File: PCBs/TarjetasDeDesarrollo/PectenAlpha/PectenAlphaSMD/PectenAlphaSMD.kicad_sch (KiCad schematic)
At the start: 26 parts, among them J1 ICSP, J2 GPIO, Q1 PN2222A, SW1 SW_Push, SW2 SW_DIP_x04, U1 PIC_8-14-18-20, U2 D148K

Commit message: Se actualizó la biblioteca de la pecten Alpha pero se harán modificaciones para el CH340 usb a ttl
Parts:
- BZ1: footprint (none) -> Buzzer_Beeper:Buzzer_12x9.5RM7.6
- D1: footprint (none) -> LED_SMD:LED_1206_3216Metric
- D10: footprint (none) -> LED_SMD:LED_RGB_5050-6
- J1: footprint (none) -> Connector_PinHeader_2.54mm:PinHeader_1x06_P2.54mm_Horizontal
- J2: footprint (none) -> Connector_PinHeader_2.54mm:PinHeader_2x12_P2.54mm_Vertical
- JP1: footprint (none) -> Jumper:SolderJumper-3_P1.3mm_Open_RoundedPad1.0x1.5mm
- R1, R10, R11, R12, R13, R14, R2, R3, R4, R5, R6, R7, R8, R9: footprint (none) -> Resistor_SMD:R_0805_2012Metric_Pad1.20x1.40mm_HandSolder
- RV1: footprint (none) -> Potentiometer_THT:Potentiometer_Runtron_RM-065_Vertical
- SW1: footprint (none) -> Button_Switch_THT:SW_PUSH_6mm_H4.3mm
- SW2: footprint (none) -> Button_Switch_THT:SW_DIP_SPSTx04_Slide_6.7x11.72mm_W7.62mm_P2.54mm_LowProfile
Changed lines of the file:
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@@
 			)
 		)
-		(property "Footprint" ""
+		(property "Footprint" "Resistor_SMD:R_0805_2012Metric_Pad1.20x1.40mm_HandSolder"
 			(at 142.494 145.796 90)
 			(effects
@@
 			)
 		)
-		(property "Footprint" ""
+		(property "Footprint" "Button_Switch_THT:SW_DIP_SPSTx04_Slide_6.7x11.72mm_W7.62mm_P2.54mm_LowProfile"
 			(at 99.06 68.58 0)
 			(effects
@@
 			)
 		)
-		(property "Footprint" ""
+		(property "Footprint" "Resistor_SMD:R_0805_2012Metric_Pad1.20x1.40mm_HandSolder"
 			(at 171.196 86.614 90)
 			(effects
@@
 			)
 		)
-		(property "Footprint" ""
+		(property "Footprint" "LED_SMD:LED_1206_3216Metric"
 			(at 114.3 115.57 0)
 			(effects
@@
 			)
 		)
-		(property "Footprint" ""
+		(property "Footprint" "Connector_PinHeader_2.54mm:PinHeader_2x12_P2.54mm_Vertical"
 			(at 105.41 163.83 0)
 			(effects
@@
 			)
 		)
-		(property "Footprint" ""
+		(property "Footprint" "Buzzer_Beeper:Buzzer_12x9.5RM7.6"
 			(at 128.905 80.01 90)
 			(effects
@@
 		(dnp no)
 		(fields_autoplaced yes)
-		(property "Reference" "#PWR?"
+		(property "Reference" "#PWR0101"
 			(at 99.06 186.69 0)
 			(effects
@@
 			(project ""
 				(path "/6ae505d1-4155-497e-9091-07ebabfd0d72"
-					(reference "#PWR?")
+					(reference "#PWR0101")
 					(unit 1)
 				)
@@
 			)
 		)
-		(property "Footprint" ""
+		(property "Footprint" "Potentiometer_THT:Potentiometer_Runtron_RM-065_Vertical"
 			(at 82.55 93.98 0)
 			(effects
@@
 			)
 		)
-		(property "Footprint" ""
+		(property "Footprint" "Jumper:SolderJumper-3_P1.3mm_Open_RoundedPad1.0x1.5mm"
 			(at 123.19 55.88 0)
 			(effects
@@
 			)
 		)
-		(property "Footprint" ""
+		(property "Footprint" "Connector_PinHeader_2.54mm:PinHeader_1x06_P2.54mm_Horizontal"
 			(at 62.23 157.48 0)
 			(effects
@@
 			)
 		)
-		(property "Footprint" ""
+		(property "Footprint" "Resistor_SMD:R_0805_2012Metric_Pad1.20x1.40mm_HandSolder"
 			(at 101.346 115.316 90)
 			(effects
@@
 			)
 		)
-		(property "Footprint" ""
+		(property "Footprint" "Resistor_SMD:R_0805_2012Metric_Pad1.20x1.40mm_HandSolder"
 			(at 142.494 155.956 90)
 			(effects
@@
 			)
 		)
-		(property "Footprint" ""
+		(property "Footprint" "Resistor_SMD:R_0805_2012Metric_Pad1.20x1.40mm_HandSolder"
 			(at 142.494 135.636 90)
 			(effects
@@
 			)
 		)
-		(property "Footprint" ""
+		(property "Footprint" "LED_SMD:LED_RGB_5050-6"
 			(at 162.56 95.25 0)
 			(effects
@@
 			)
 		)
-		(property "Footprint" ""
+		(property "Footprint" "Resistor_SMD:R_0805_2012Metric_Pad1.20x1.40mm_HandSolder"
 			(at 142.494 166.116 90)
 			(effects
@@
 			)
 		)
-		(property "Footprint" ""
+		(property "Footprint" "Resistor_SMD:R_0805_2012Metric_Pad1.20x1.40mm_HandSolder"
 			(at 142.494 125.476 90)
 			(effects
@@
 			)
 		)
-		(property "Footprint" ""
+		(property "Footprint" "Resistor_SMD:R_0805_2012Metric_Pad1.20x1.40mm_HandSolder"
 			(at 142.494 115.316 90)
 			(effects
@@
 			)
 		)
-		(property "Footprint" ""
+		(property "Footprint" "Button_Switch_THT:SW_PUSH_6mm_H4.3mm"
 			(at 95.25 127 0)
 			(effects
@@
 			)
 		)
-		(property "Footprint" ""
+		(property "Footprint" "Resistor_SMD:R_0805_2012Metric_Pad1.20x1.40mm_HandSolder"
 			(at 142.494 176.276 90)
 			(effects
@@
 			)
 		)
-		(property "Footprint" ""
+		(property "Footprint" "Resistor_SMD:R_0805_2012Metric_Pad1.20x1.40mm_HandSolder"
 			(at 142.494 186.436 90)
 			(effects
@@
 			)
 		)
-		(property "Footprint" ""
+		(property "Footprint" "Resistor_SMD:R_0805_2012Metric_Pad1.20x1.40mm_HandSolder"
 			(at 162.306 86.614 90)
 			(effects
@@
 			)
 		)
-		(property "Footprint" ""
+		(property "Footprint" "Resistor_SMD:R_0805_2012Metric_Pad1.20x1.40mm_HandSolder"
 			(at 153.416 86.614 90)
 			(effects
@@
 			)
 		)
-		(property "Footprint" ""
+		(property "Footprint" "Resistor_SMD:R_0805_2012Metric_Pad1.20x1.40mm_HandSolder"
 			(at 115.316 127.254 90)
 			(effects
@@
 			)
 		)
-		(property "Footprint" ""
+		(property "Footprint" "Resistor_SMD:R_0805_2012Metric_Pad1.20x1.40mm_HandSolder"
 			(at 115.316 89.154 90)
 			(effects

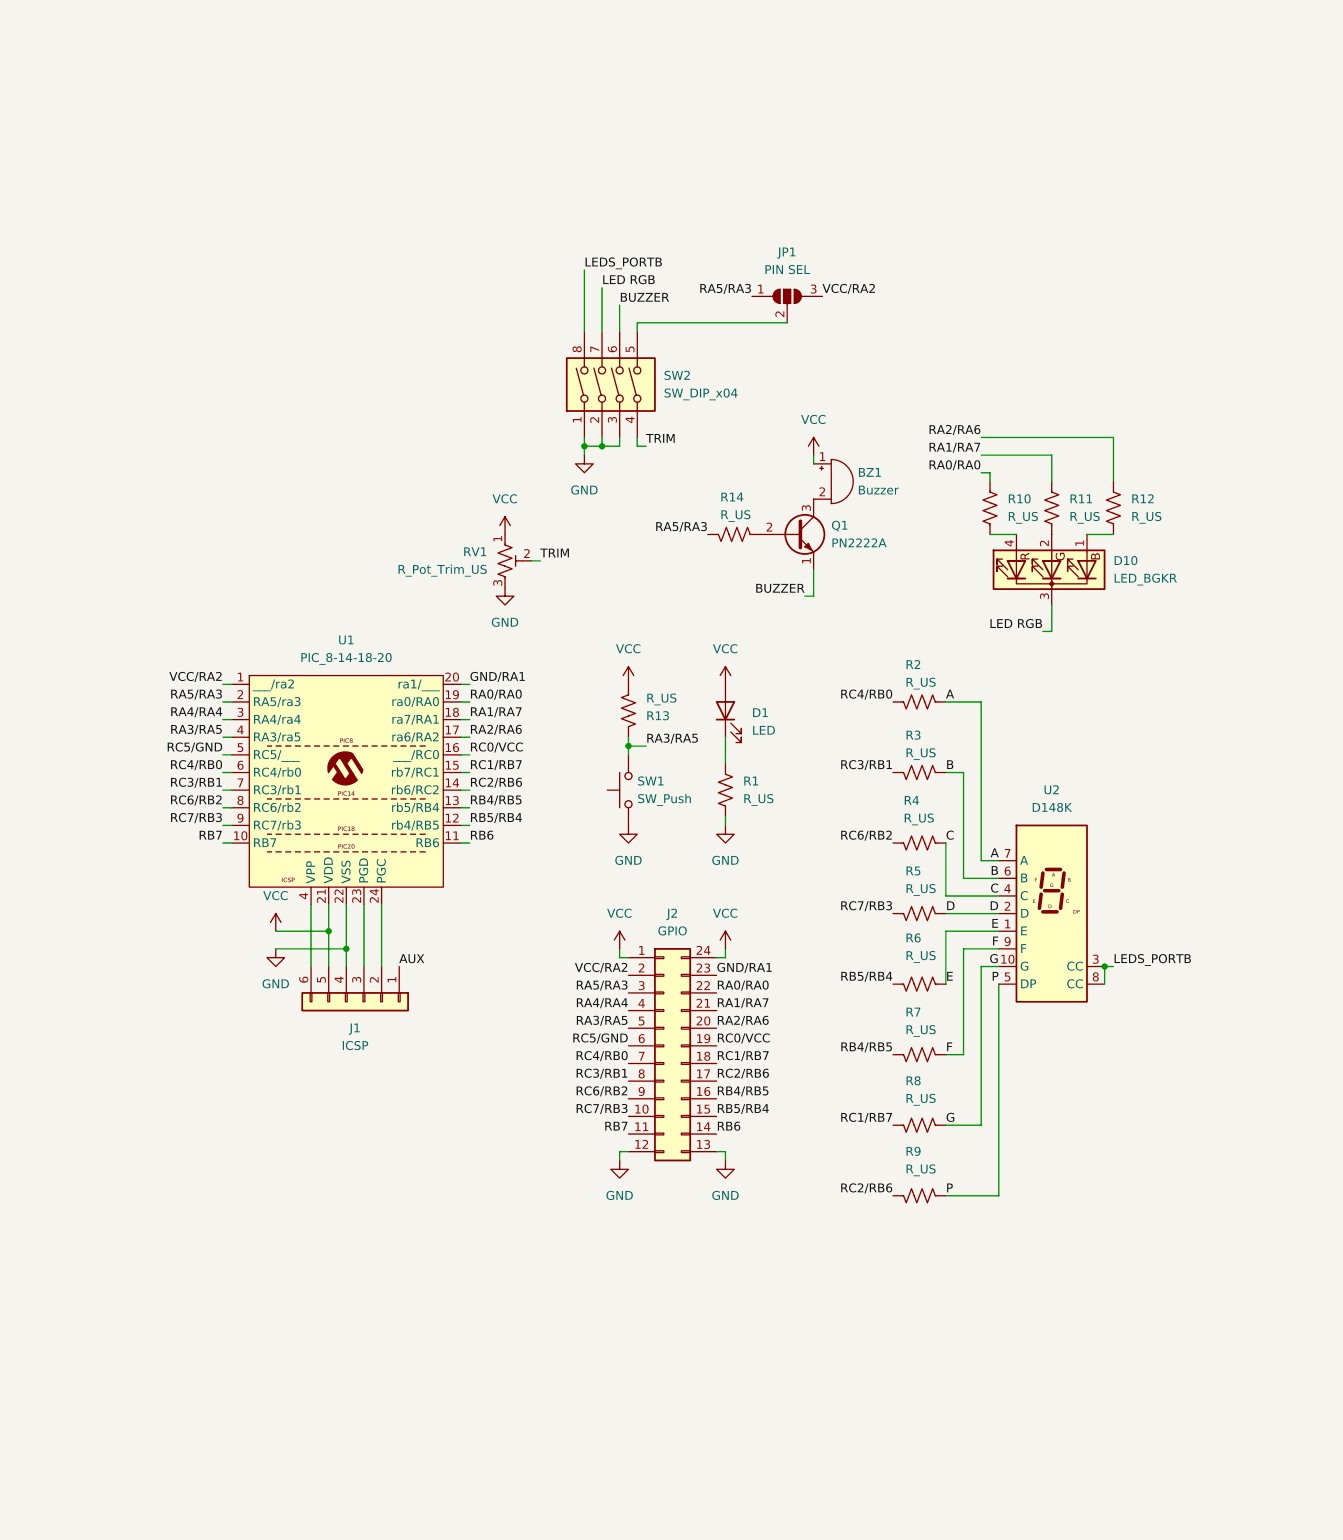
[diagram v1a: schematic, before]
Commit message: Se tiene la PCB preliminar con forma de pecten alpha
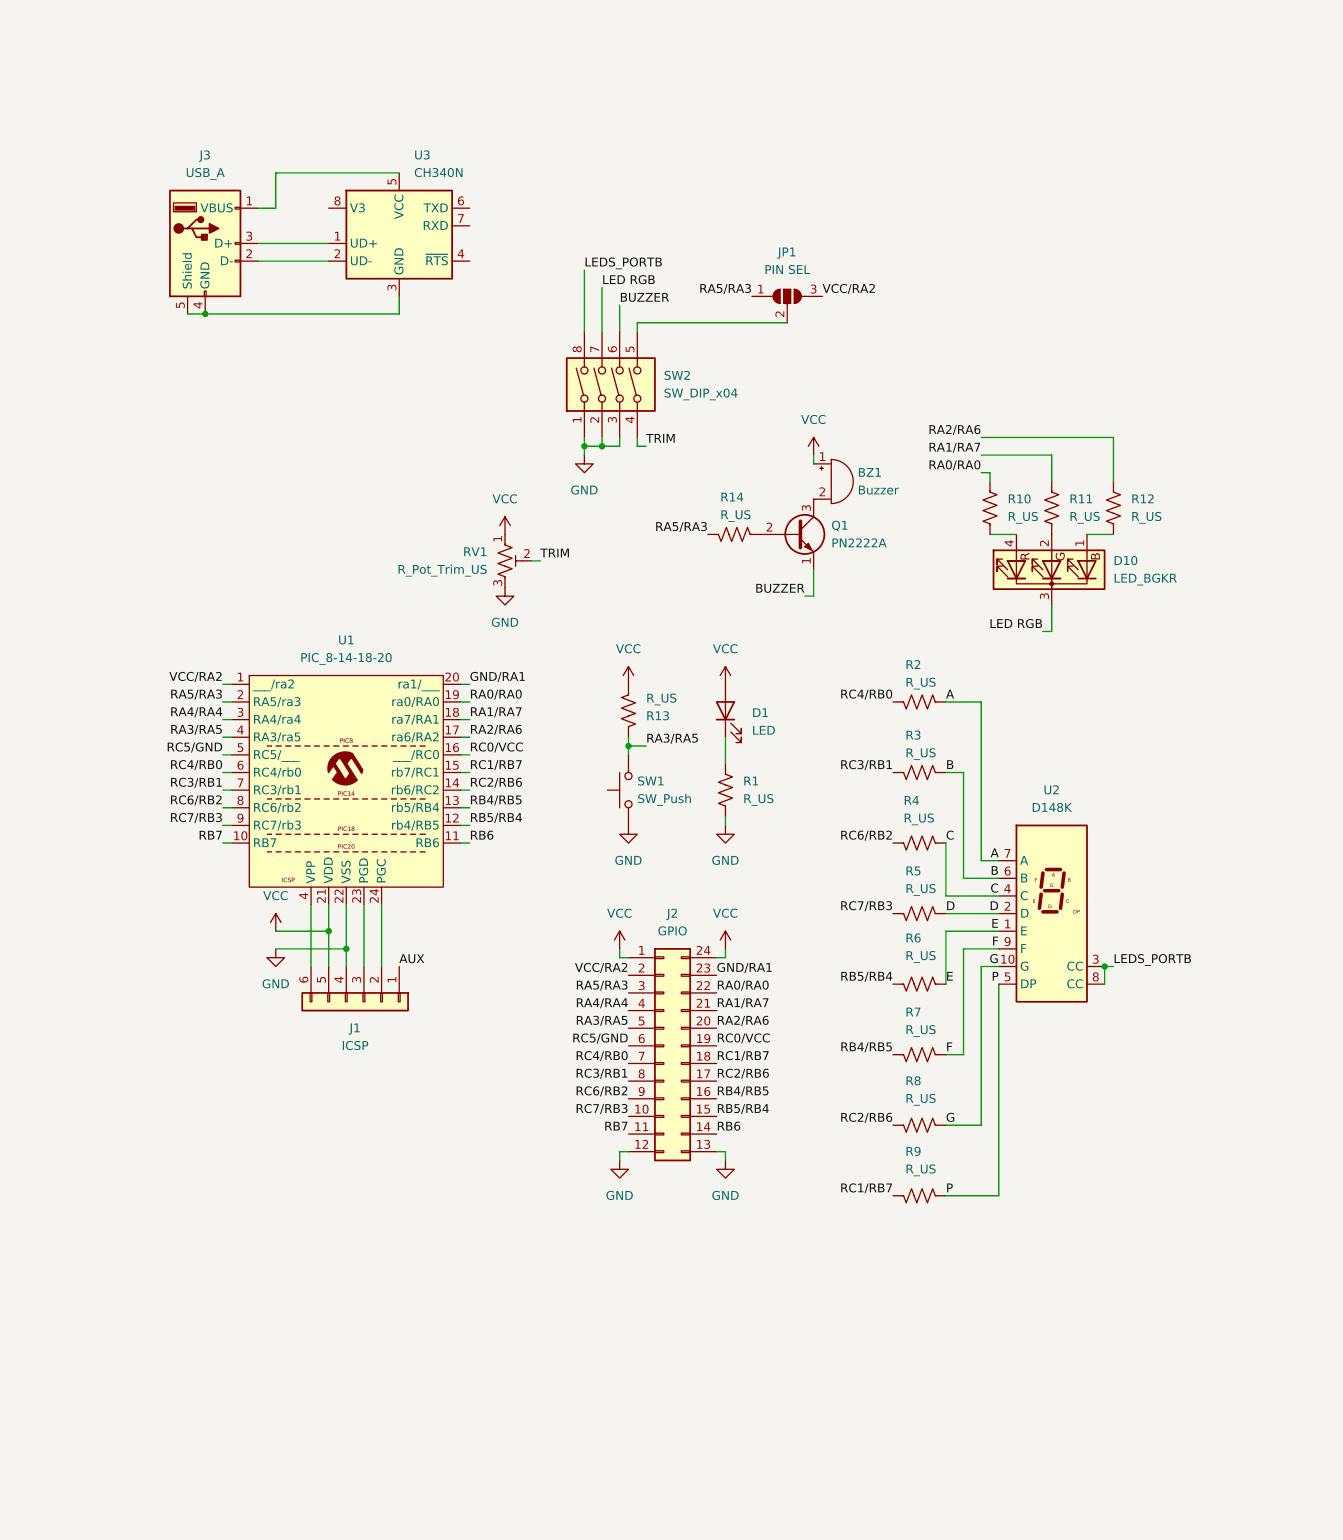
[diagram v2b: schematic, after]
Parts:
- added J3: USB_A, Connector_USB:USB_A_CNCTech_1001-011-01101_Horizontal, symbol Connector:USB_A
- added U3: CH340N, Package_SO:JEITA_SOIC-8_3.9x4.9mm_P1.27mm, symbol Interface_USB:CH340N
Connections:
- net RC1/RB7: now also R9.1; no longer R8.1
- net RC2/RB6: now also R8.1; no longer R9.1
- new net: J3.3 (D+), U3.1 (UD+)
- new net: J3.2 (D-), U3.2 (UD-)
- new net: J3.4 (GND), J3.5 (Shield), U3.3 (GND)
- new net: J3.1 (VBUS), U3.5 (VCC)
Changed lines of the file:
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@@
 	)
 	(junction
+		(at 39.37 58.42)
+		(diameter 0)
+		(color 0 0 0 0)
+	)
+	(junction
 		(at 93.98 77.47)
 		(diameter 0)
@@
 	(wire
 		(pts
+			(xy 49.53 38.1) (xy 67.31 38.1)
+		)
+		(stroke
+			(width 0)
+			(type default)
+		)
+	)
+	(wire
+		(pts
 			(xy 41.91 127) (xy 43.18 127)
 		)
@@
 	(wire
 		(pts
+			(xy 46.99 48.26) (xy 57.15 48.26)
+		)
+		(stroke
+			(width 0)
+			(type default)
+		)
+	)
+	(wire
+		(pts
 			(xy 153.67 147.32) (xy 146.05 147.32)
 		)
@@
 	(wire
 		(pts
+			(xy 46.99 50.8) (xy 57.15 50.8)
+		)
+		(stroke
+			(width 0)
+			(type default)
+		)
+	)
+	(wire
+		(pts
 			(xy 151.13 175.26) (xy 146.05 175.26)
 		)
@@
 	(wire
 		(pts
+			(xy 67.31 58.42) (xy 39.37 58.42)
+		)
+		(stroke
+			(width 0)
+			(type default)
+		)
+	)
+	(wire
+		(pts
 			(xy 153.67 149.86) (xy 148.59 149.86)
 		)
@@
 	(wire
 		(pts
+			(xy 36.83 58.42) (xy 39.37 58.42)
+		)
+		(stroke
+			(width 0)
+			(type default)
+		)
+	)
+	(wire
+		(pts
 			(xy 146.05 142.24) (xy 146.05 134.62)
 		)
@@
 	(wire
 		(pts
+			(xy 67.31 55.88) (xy 67.31 58.42)
+		)
+		(stroke
+			(width 0)
+			(type default)
+		)
+	)
+	(wire
+		(pts
 			(xy 93.98 77.47) (xy 96.52 77.47)
 		)
@@
 	(wire
 		(pts
+			(xy 49.53 43.18) (xy 49.53 38.1)
+		)
+		(stroke
+			(width 0)
+			(type default)
+		)
+	)
+	(wire
+		(pts
 			(xy 77.47 127) (xy 76.2 127)
 		)
@@
 	(wire
 		(pts
+			(xy 46.99 43.18) (xy 49.53 43.18)
+		)
+		(stroke
+			(width 0)
+			(type default)
+		)
+	)
+	(wire
+		(pts
 			(xy 151.13 137.16) (xy 151.13 114.3)
 		)
@@
 	)
 	(label "RC2{slash}RB6"
-		(at 138.43 185.42 180)
+		(at 138.43 175.26 180)
 		(effects
 			(font
@@
 	)
 	(label "RC1{slash}RB7"
-		(at 138.43 175.26 180)
+		(at 138.43 185.42 180)
 		(effects
 			(font
@@
 	)
 	(symbol
+		(lib_id "Interface_USB:CH340N")
+		(at 67.31 45.72 0)
+		(unit 1)
+		(exclude_from_sim no)
+		(in_bom yes)
+		(on_board yes)
+		(dnp no)
+		(property "Reference" "U3"
+			(at 69.4533 35.56 0)
+			(effects
+				(font
+					(size 1.27 1.27)
+				)
+				(justify left)
+			)
+		)
+		(property "Value" "CH340N"
+			(at 69.4533 38.1 0)
+			(effects
+				(font
+					(size 1.27 1.27)
+				)
+				(justify left)
+			)
+		)
+		(property "Footprint" "Package_SO:JEITA_SOIC-8_3.9x4.9mm_P1.27mm"
+			(at 63.5 26.67 0)
+			(effects
+				(font
+					(size 1.27 1.27)
+				)
+				(hide yes)
+			)
+		)
+		(property "Datasheet" "https://aitendo3.sakura.ne.jp/aitendo_data/product_img/ic/inteface/CH340N/ch340n.pdf"
+			(at 64.77 40.64 0)
+			(effects
+				(font
+					(size 1.27 1.27)
+				)
+				(hide yes)
+			)
+		)
+		(property "Description" "USB serial converter, 2Mbps, UART, JEITA SOIC-8 (SOP-8)"
+			(at 67.31 45.72 0)
+			(effects
+				(font
+					(size 1.27 1.27)
+				)
+				(hide yes)
+			)
+		)
+		(pin "7"
+		)
+		(pin "8"
+		)
+		(pin "6"
+		)
+		(pin "1"
+		)
+		(pin "5"
+		)
+		(pin "3"
+		)
+		(pin "4"
+		)
+		(pin "2"
+		)
+		(instances
+			(project ""
+				(path "/6ae505d1-4155-497e-9091-07ebabfd0d72"
+					(reference "U3")
+					(unit 1)
+				)
+			)
+		)
+	)
+	(symbol
 		(lib_id "Device:R_US")
 		(at 142.24 124.46 90)
@@
 					(unit 1)
 				)
+			)
+		)
+	)
+	(symbol
+		(lib_id "Connector:USB_A")
+		(at 39.37 48.26 0)
+		(unit 1)
+		(exclude_from_sim no)
+		(in_bom yes)
+		(on_board yes)
+		(dnp no)
+		(fields_autoplaced yes)
+		(property "Reference" "J3"
+			(at 39.37 35.56 0)
+			(effects
+				(font
+					(size 1.27 1.27)
+				)
+			)
+		)
+		(property "Value" "USB_A"
+			(at 39.37 38.1 0)
+			(effects
+				(font
+					(size 1.27 1.27)
+				)
+			)
+		)
+		(property "Footprint" "Connector_USB:USB_A_CNCTech_1001-011-01101_Horizontal"
+			(at 43.18 49.53 0)
+			(effects
+				(font
+					(size 1.27 1.27)
+				)
+				(hide yes)
+			)
+		)
+		(property "Datasheet" "~"
+			(at 43.18 49.53 0)
+			(effects
+				(font
+					(size 1.27 1.27)
+				)
+				(hide yes)
+			)
+		)
+		(property "Description" "USB Type A connector"
+			(at 39.37 48.26 0)
+			(effects
+				(font
+					(size 1.27 1.27)
+				)
+				(hide yes)
+			)
+		)
+		(pin "3"
+		)
+		(pin "1"
+		)
+		(pin "2"
+		)
+		(pin "5"
+		)
+		(pin "4"
+		)
+		(instances
+			(project ""
+				(path "/6ae505d1-4155-497e-9091-07ebabfd0d72"
+					(reference "J3")
+					(unit 1)
+				)
